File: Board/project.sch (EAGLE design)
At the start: 16 parts, among them U1 ATMEGA328P_PDIP

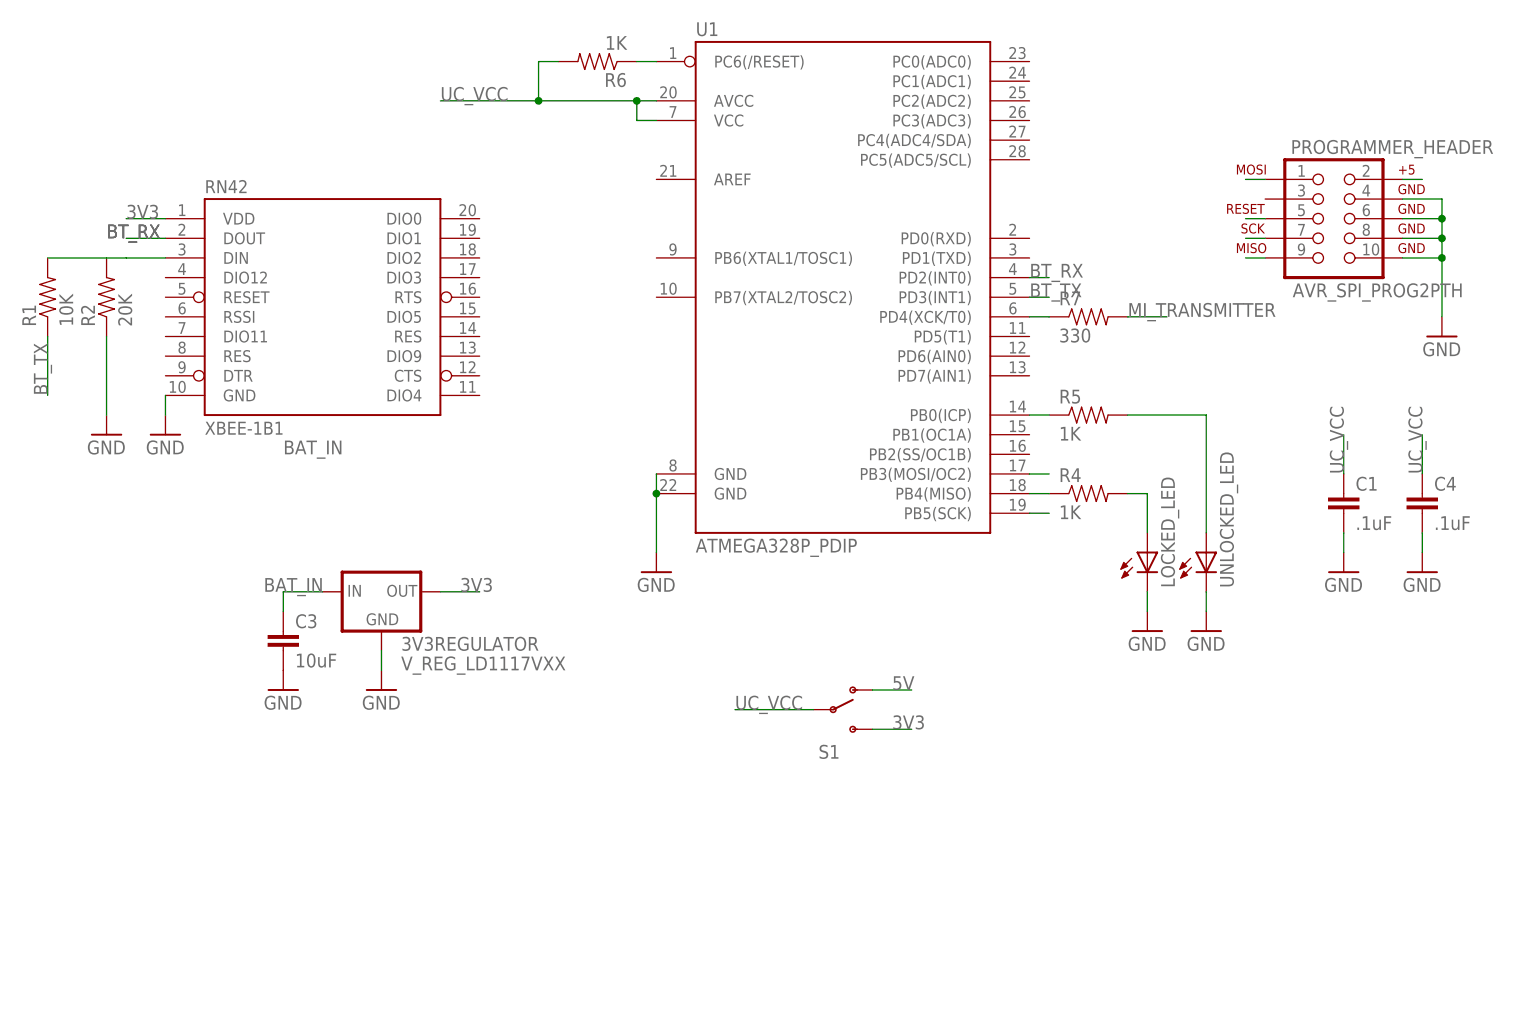
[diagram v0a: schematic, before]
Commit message: Added pads for MI transmitter and battery power, plus PCB layout.
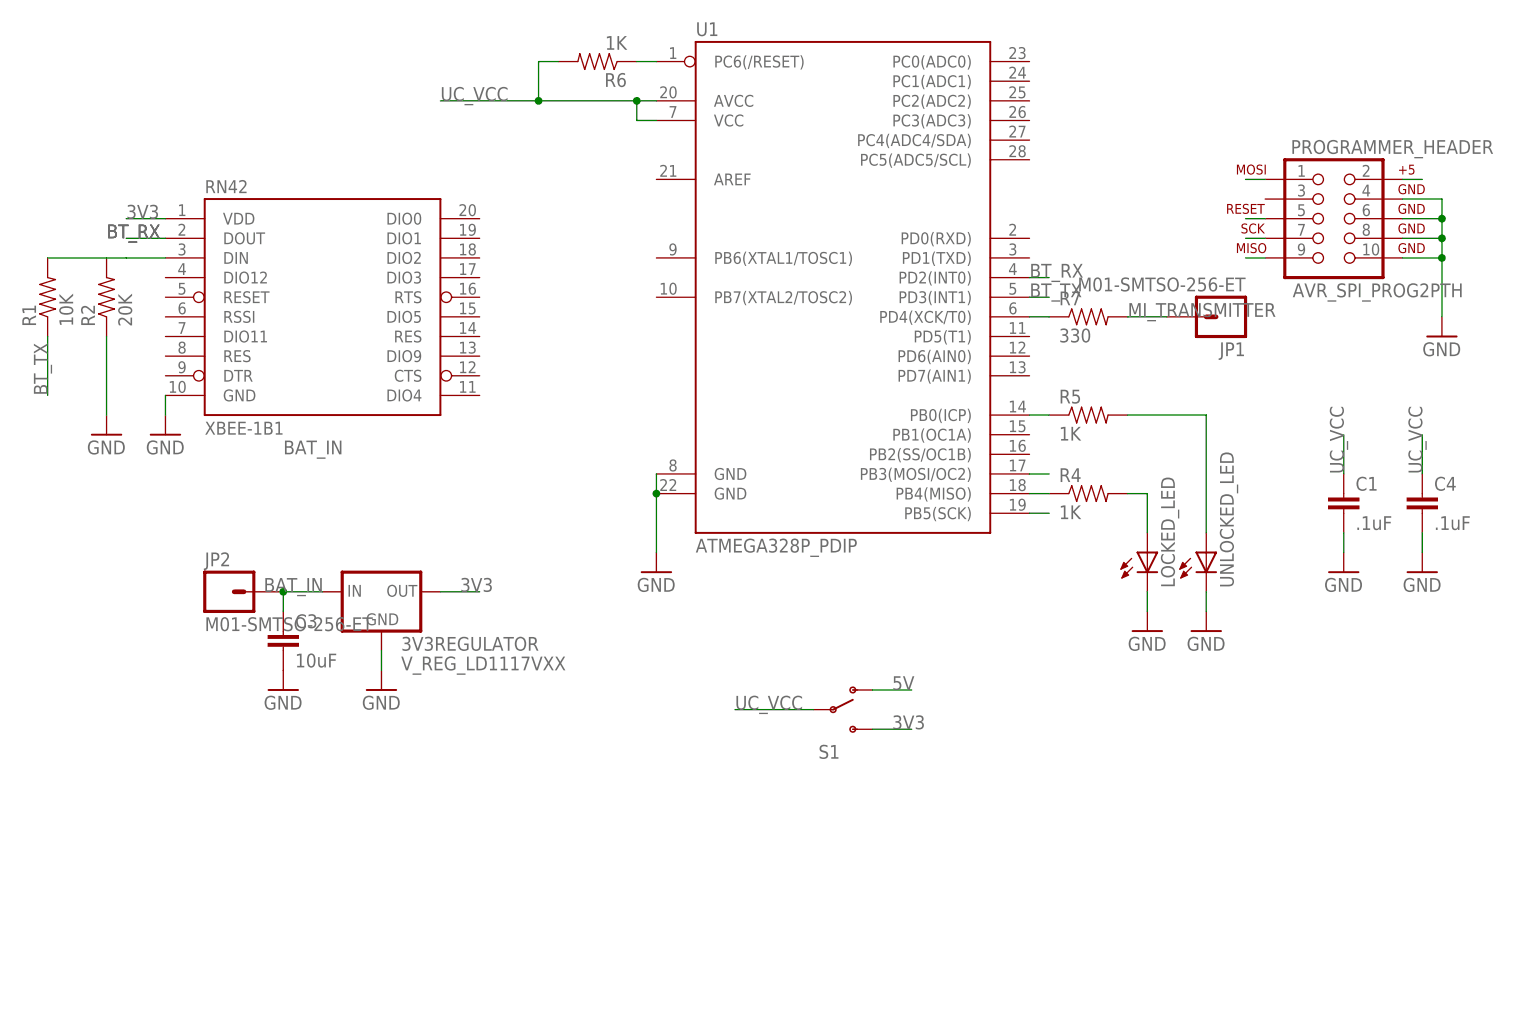
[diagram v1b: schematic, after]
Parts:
- added JP1, JP2: M01-SMTSO-256-ET, SparkFun-Connectors:M01-SMTSO-256-ET
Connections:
- net BAT_IN: now also JP2.1
- net MI_TRANSMITTER: now also JP1.1
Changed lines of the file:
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@@
 <part name="GND9" library="SparkFun-Aesthetics" deviceset="GND" device=""/>
 <part name="GND10" library="SparkFun-Aesthetics" deviceset="GND" device=""/>
+<part name="JP1" library="SparkFun-Connectors" deviceset="M01" device="-SMTSO-256-ET"/>
+<part name="JP2" library="SparkFun-Connectors" deviceset="M01" device="-SMTSO-256-ET"/>
 </parts>
 <sheets>
@@
 <instance part="GND9" gate="1" x="81.28" y="55.88"/>
 <instance part="GND10" gate="1" x="-66.04" y="40.64"/>
+<instance part="JP1" gate="G$1" x="55.88" y="88.9" rot="R180"/>
+<instance part="JP2" gate="G$1" x="-73.66" y="53.34"/>
 </instances>
 <busses>
@@
 <label x="-66.04" y="71.12" size="1.778" layer="95"/>
 <label x="-68.58" y="53.34" size="1.778" layer="95"/>
+<pinref part="JP2" gate="G$1" pin="1"/>
+<junction x="-66.04" y="53.34"/>
 </segment>
 </net>
@@
 <wire x1="43.18" y1="88.9" x2="48.26" y2="88.9" width="0.1524" layer="91"/>
 <label x="43.18" y="88.9" size="1.778" layer="95"/>
-</segment>
-</net>
+<pinref part="JP1" gate="G$1" pin="1"/>
+</segment>
+</net>

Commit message: Changed some pins for better routing, passes DRC now.
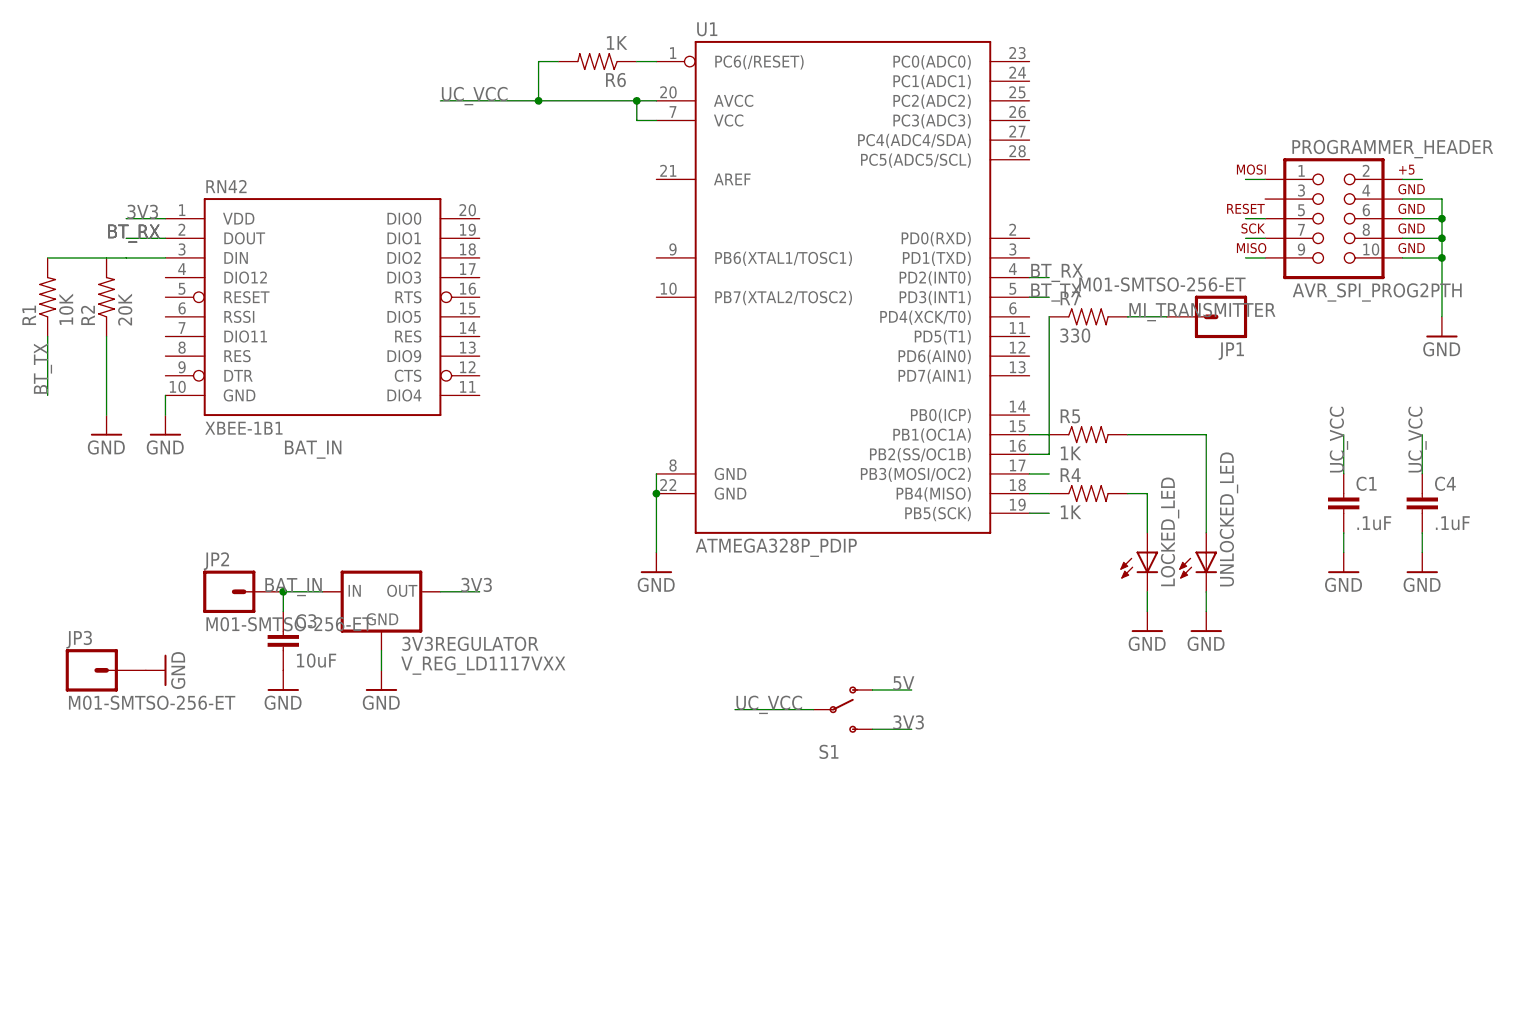
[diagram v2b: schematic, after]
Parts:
- added JP3: M01-SMTSO-256-ET, SparkFun-Connectors:M01-SMTSO-256-ET
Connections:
- removed net N$4: R7.1, U1.PD4(XCK/T0)
- new net N$3: R7.1, U1.PB2(SS/OC1B)
- net GND: now also JP3.1
- net N$2: now also U1.PB1(OC1A); no longer U1.PB0(ICP)
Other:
- moved on the sheet: R5
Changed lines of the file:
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@@
 <part name="JP1" library="SparkFun-Connectors" deviceset="M01" device="-SMTSO-256-ET"/>
 <part name="JP2" library="SparkFun-Connectors" deviceset="M01" device="-SMTSO-256-ET"/>
+<part name="JP3" library="SparkFun-Connectors" deviceset="M01" device="-SMTSO-256-ET"/>
+<part name="GND11" library="SparkFun-Aesthetics" deviceset="GND" device=""/>
 </parts>
 <sheets>
@@
 <instance part="R2" gate="G$1" x="-88.9" y="91.44" rot="R90"/>
 <instance part="R4" gate="G$1" x="38.1" y="66.04"/>
-<instance part="R5" gate="G$1" x="38.1" y="76.2"/>
+<instance part="R5" gate="G$1" x="38.1" y="73.66"/>
 <instance part="R6" gate="G$1" x="-25.4" y="121.92" rot="R180"/>
 <instance part="C1" gate="G$1" x="71.12" y="63.5"/>
@@
 <instance part="JP1" gate="G$1" x="55.88" y="88.9" rot="R180"/>
 <instance part="JP2" gate="G$1" x="-73.66" y="53.34"/>
+<instance part="JP3" gate="G$1" x="-91.44" y="43.18"/>
+<instance part="GND11" gate="1" x="-81.28" y="43.18" rot="R90"/>
 </instances>
 <busses>
@@
 <pinref part="GND10" gate="1" pin="GND"/>
 </segment>
+<segment>
+<pinref part="JP3" gate="G$1" pin="1"/>
+<pinref part="GND11" gate="1" pin="GND"/>
+</segment>
 </net>
 <net name="UC_VCC" class="0">
@@
 </segment>
 </net>
-<net name="N$2" class="0">
-<segment>
-<pinref part="U1" gate="G$1" pin="PB0(ICP)"/>
-<wire x1="30.48" y1="76.2" x2="33.02" y2="76.2" width="0.1524" layer="91"/>
-<pinref part="R5" gate="G$1" pin="1"/>
-</segment>
-</net>
 <net name="MISO" class="0">
 <segment>
@@
 <segment>
 <pinref part="R5" gate="G$1" pin="2"/>
-<wire x1="43.18" y1="76.2" x2="53.34" y2="76.2" width="0.1524" layer="91"/>
+<wire x1="43.18" y1="73.66" x2="53.34" y2="73.66" width="0.1524" layer="91"/>
 <pinref part="UNLOCKED_LED" gate="G$1" pin="A"/>
-<wire x1="53.34" y1="76.2" x2="53.34" y2="60.96" width="0.1524" layer="91"/>
+<wire x1="53.34" y1="73.66" x2="53.34" y2="60.96" width="0.1524" layer="91"/>
 </segment>
 </net>
@@
 </segment>
 </net>
-<net name="N$4" class="0">
-<segment>
-<pinref part="U1" gate="G$1" pin="PD4(XCK/T0)"/>
-<wire x1="30.48" y1="88.9" x2="33.02" y2="88.9" width="0.1524" layer="91"/>
-<pinref part="R7" gate="G$1" pin="1"/>
-</segment>
-</net>
 <net name="MI_TRANSMITTER" class="0">
 <segment>
@@
 </segment>
 </net>
+<net name="N$2" class="0">
+<segment>
+<pinref part="U1" gate="G$1" pin="PB1(OC1A)"/>
+<pinref part="R5" gate="G$1" pin="1"/>
+<wire x1="30.48" y1="73.66" x2="33.02" y2="73.66" width="0.1524" layer="91"/>
+</segment>
+</net>
+<net name="N$3" class="0">
+<segment>
+<pinref part="U1" gate="G$1" pin="PB2(SS/OC1B)"/>
+<wire x1="30.48" y1="71.12" x2="33.02" y2="71.12" width="0.1524" layer="91"/>
+<pinref part="R7" gate="G$1" pin="1"/>
+<wire x1="33.02" y1="71.12" x2="33.02" y2="88.9" width="0.1524" layer="91"/>
+</segment>
+</net>
